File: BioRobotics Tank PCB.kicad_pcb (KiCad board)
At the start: 2 copper layers, 72 x 90 mm, 72 parts, among them J1 Conn_01x02, J2 Conn_01x02, J3 Conn_01x02, J4 Conn_01x02, J5 Conn_01x02, J6 Conn_01x02, J7 Conn_01x02, J8 Conn_02x05_Odd_Even, J9 Conn_01x05, Q1 IPD060N03LGATMA1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

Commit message: Change ideal diode mosfet and increase track sizes
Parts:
- Q1: value IPD060N03LGATMA1 -> PSMN4R5-30YLC; footprint IPD060N03LGATMA1:IPD060N03LGATMA1 -> Package_TO_SOT_SMD:LFPAK56
- moved R11 12.8 mm to (157.2, 81.5)
- moved U8 9.13 mm to (152.0, 81.0), turned to 0 degrees
- moved C27 6.97 mm to (146.5, 82.5), turned to 0 degrees
- moved Q1 1.24 mm to (151.6, 76.5), turned to 0 degrees
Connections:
- Q1 pad 1: Net-(Q1-G) -> +BATT
- Q1 pad 2: VBUS -> +BATT
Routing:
- net Net-(Q1-G): track 11.7 -> 4.52 mm
- net VBUS: track 15.9 -> 9.43 mm, vias 0 -> 10
- net Net-(U8-Vdd): track 7.42 -> 10.5 mm
- net GND1: track 237.2 -> 234.2 mm, vias 247 -> 248
- net +BATT: track 2.46 -> 3.55 mm
- net Vdrive: vias 45 -> 56
- added copper zone on B.Cu, net VBUS

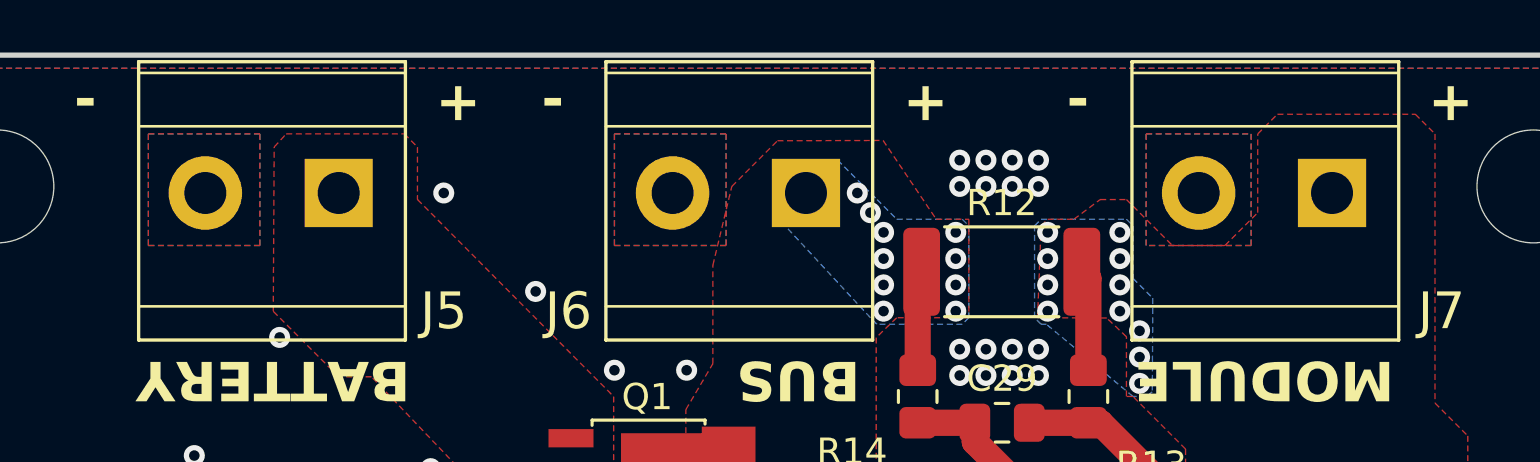
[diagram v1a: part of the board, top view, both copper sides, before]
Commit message: Add via's around power connectors to improve current capacity
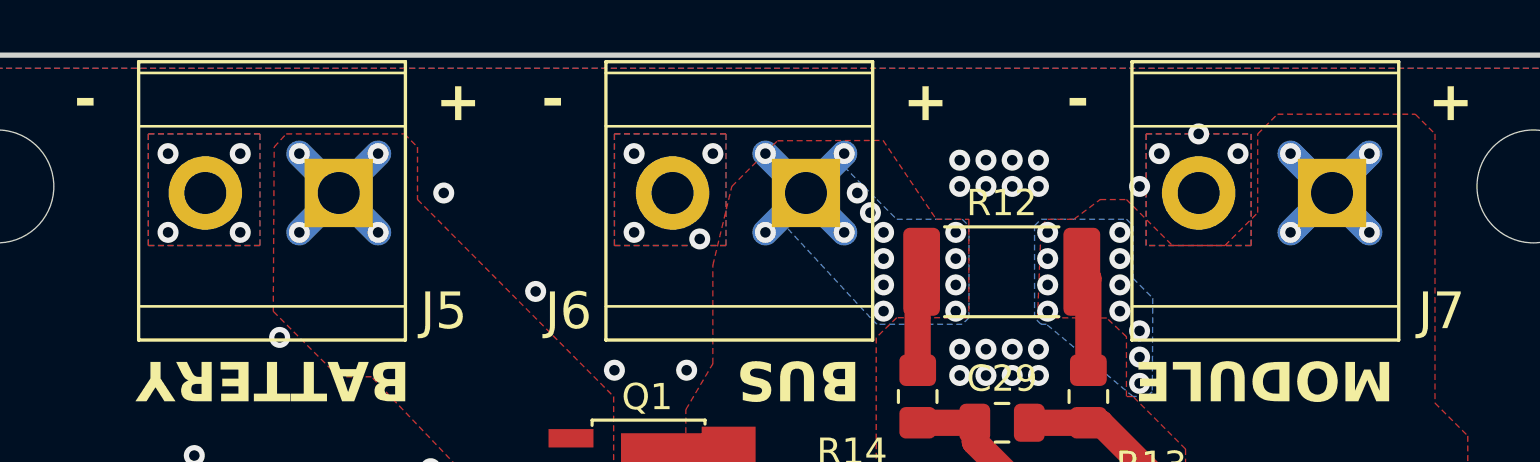
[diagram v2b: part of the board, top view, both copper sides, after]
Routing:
- net Vdrive: track 169.1 -> 177.6 mm, vias 56 -> 60
- net VBUS: track 9.43 -> 17.9 mm, vias 10 -> 14
- net +BATT: track 3.55 -> 12.0 mm, vias 0 -> 4
- net GND1: vias 248 -> 260
